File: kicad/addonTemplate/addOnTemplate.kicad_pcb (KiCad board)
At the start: 2 copper layers, 60.6 x 100 mm, 4 parts, among them J1 QTE-020-01-X-D-A

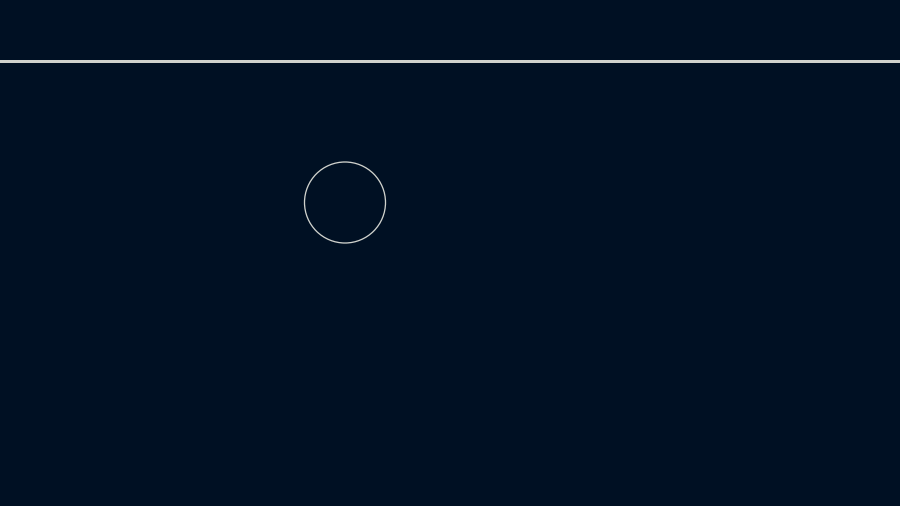
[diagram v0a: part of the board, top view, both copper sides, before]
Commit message: Added 2 add-on boards and updated GECKO5 to support olimex camera-OV7670 and an RTC.
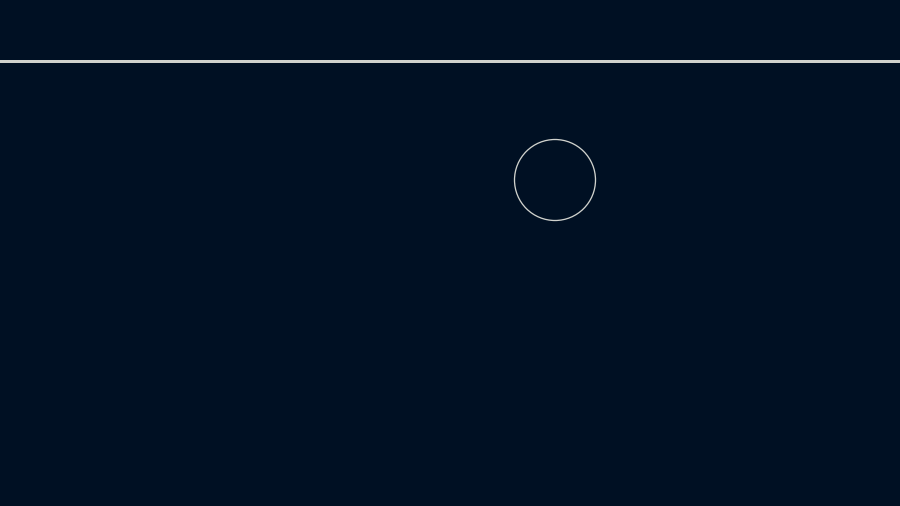
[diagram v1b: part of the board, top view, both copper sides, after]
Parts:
- moved REF** 7.04 mm to (125.2, 44.0)
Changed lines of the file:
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@@
   )
   (footprint "MountingHole:MountingHole_2.7mm_M2.5" (layer "F.Cu")
-    (at 118.2 44.7)
+    (at 125.2 43.95)
     (descr "Mounting Hole 2.7mm, no annular, M2.5")
     (tags "mounting hole 2.7mm no annular m2.5")
